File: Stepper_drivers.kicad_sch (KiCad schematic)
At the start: 9 parts, among them J7 ${STEPGEN_CH1_NAME}_STEP_AND_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, J8 ${STEPGEN_CH2_NAME}_STEP_AND_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, U5 ADuM1200AR, U6 ADuM1200AR, U7 HT26LS31ARZ

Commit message: tidy of some sheets. Added 0-10V DAC, but untested - only some basic validation on simulator for now
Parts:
- U7: footprint Package_SO:SOIC-16_3.9x9.9mm_P1.27mm -> Package_DIP:SMDIP-4_W9.53mm
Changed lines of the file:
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@@
 			)
 		)
-		(property "Footprint" "Package_SO:SOIC-16_3.9x9.9mm_P1.27mm"
+		(property "Footprint" "Package_DIP:SMDIP-4_W9.53mm"
 			(at 195.58 118.11 0)
 			(effects

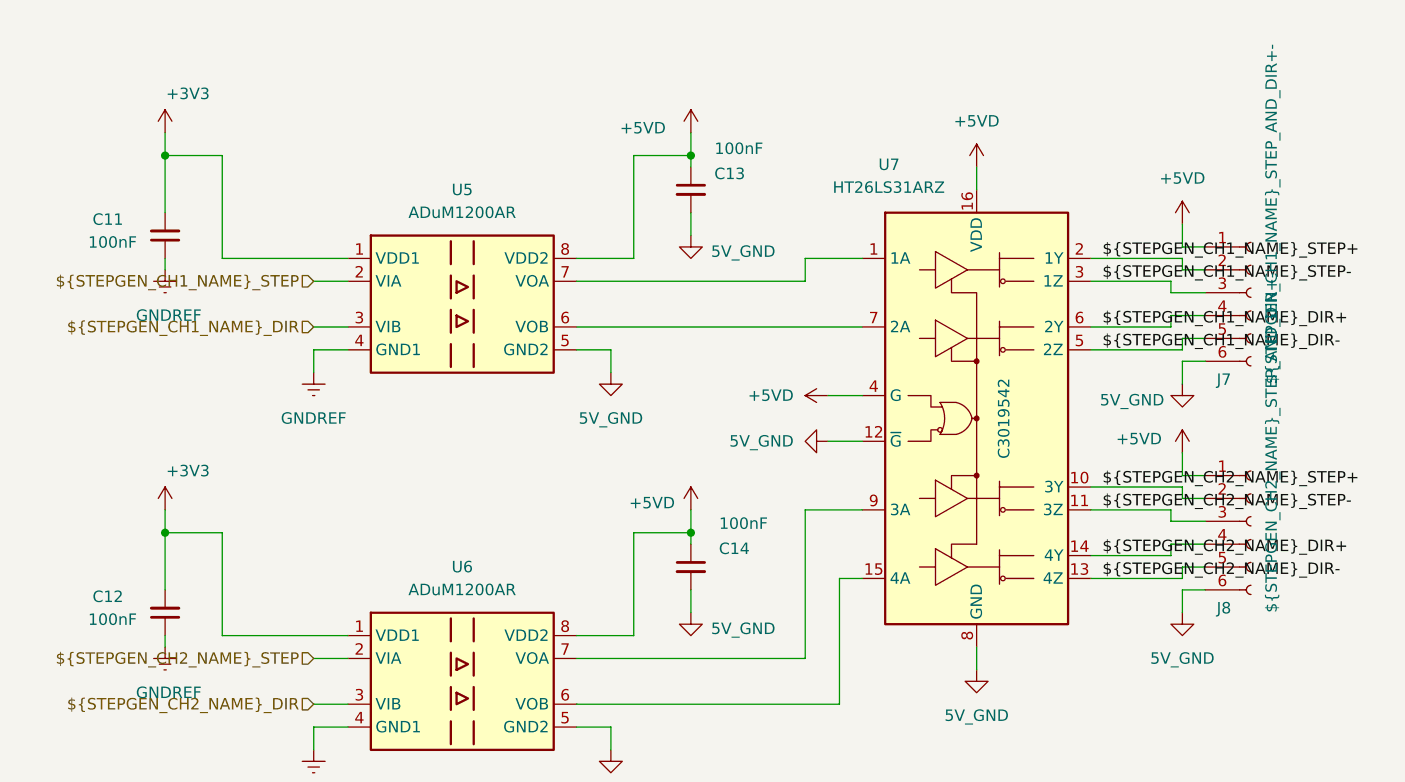
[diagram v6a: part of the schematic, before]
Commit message: Deleted stale test production files. Fixed up a bug with power isolation. Created some footprints for wire to board connectors although ran out of time to fix a bug where they do no lock in. Fixes to readme
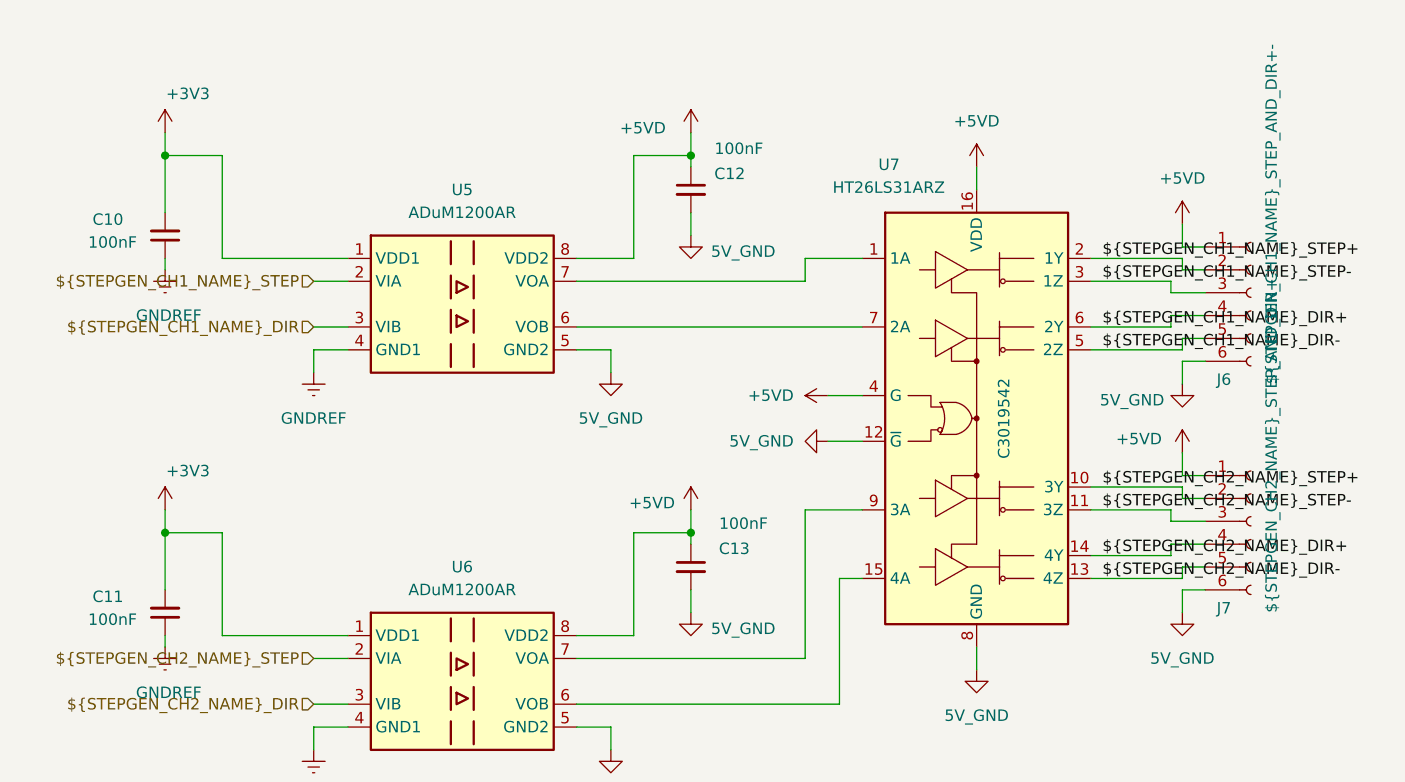
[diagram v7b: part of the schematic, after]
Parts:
- J6: renamed from J7; footprint (none) -> OSTVTerminalBlocks:Conn01x06
- J7: renamed from J8; footprint (none) -> OSTVTerminalBlocks:Conn01x06
- renumbered C11 to C10, C12 to C11, C13 to C12, C14 to C13

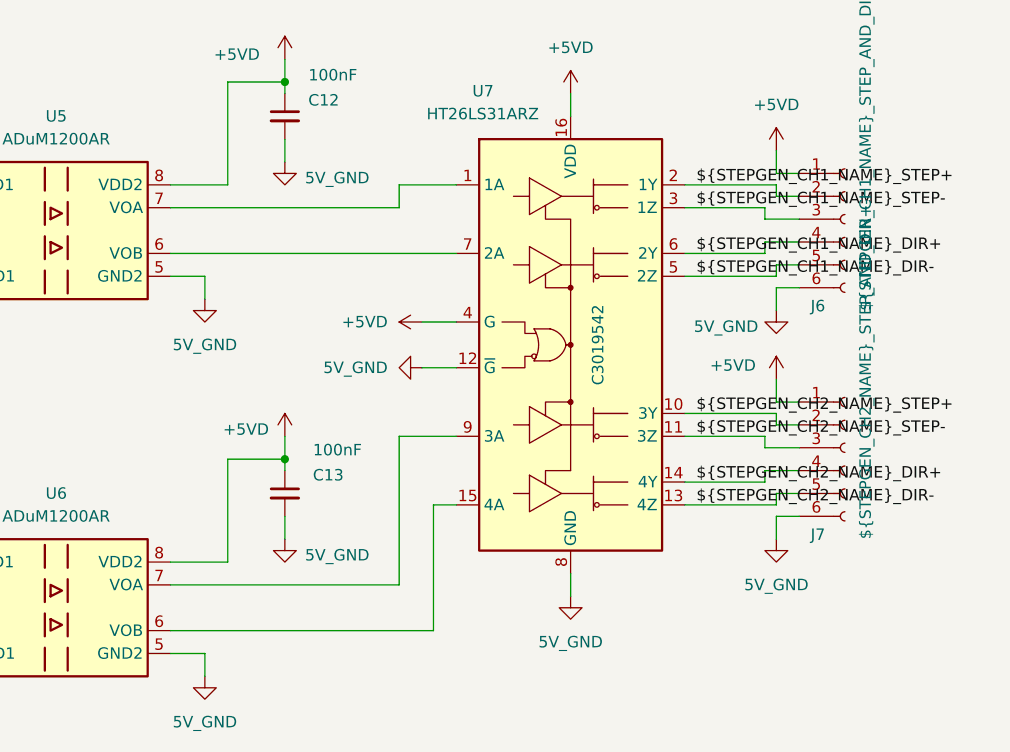
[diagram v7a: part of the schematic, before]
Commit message: restructured power supplies to enable Spindle DAC to be isolated. We now have the option of supplying two 24V inputs, one to power the nucleo and everything logic side and the other to power peripherals. Some testing will be required.
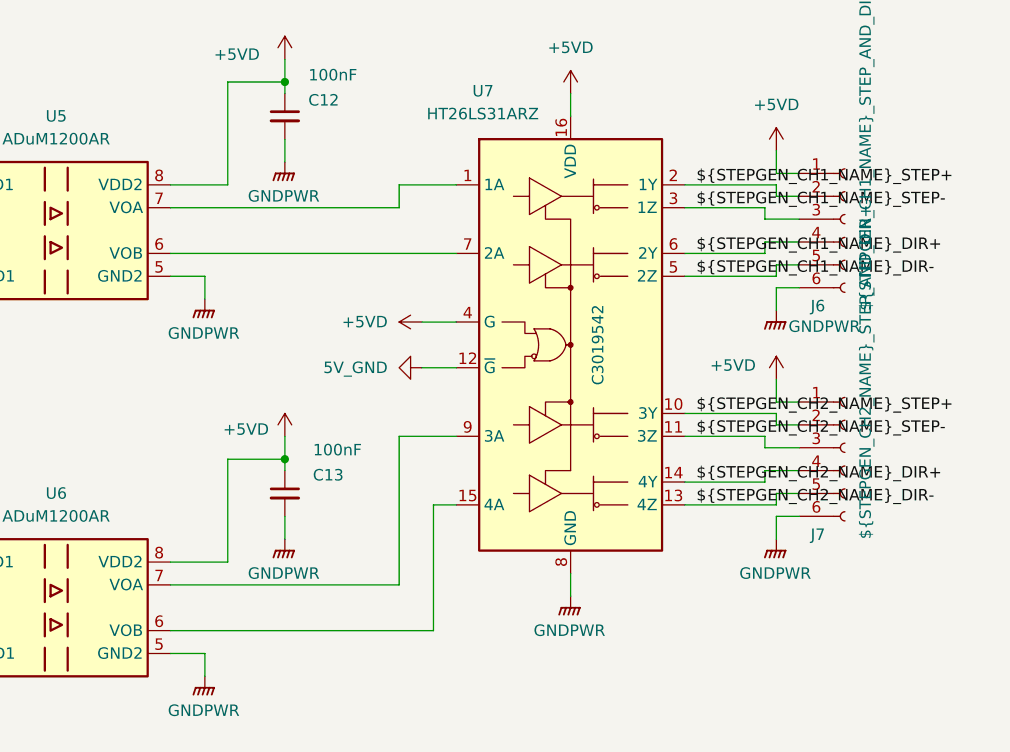
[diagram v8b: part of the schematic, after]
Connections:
- net 5V_GND: no longer C12.2, C13.2, J6.6 (Pin_6), J7.6 (Pin_6), U5.5 (GND2), U6.5 (GND2), U7.8 (GND)
- new net GNDPWR: C12.2, C13.2, J6.6 (Pin_6), J7.6 (Pin_6), U5.5 (GND2), U6.5 (GND2), U7.8 (GND)
